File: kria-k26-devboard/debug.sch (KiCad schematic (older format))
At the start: 69 parts, among them J8 1050170001, J9 0878311420, Q10 BSS138-7-F, Q11 BSS138-7-F, Q9 BSS138-7-F, U28 MCP1799-3302H_DB, U29 MCP1799-3302H_DB, U30 FT4232HPQ, U31 93LC56CT-IMC, U32 SN74AVC4T245PWR, U33 SN74AVC4T245PWR, U34 SN74AVC2T245RSWR, U35 SN74AVC2T245RSWR, U36 NC7WZ07P6X, Y5 ABM8G-12.000MHZ-18-D2Y-T

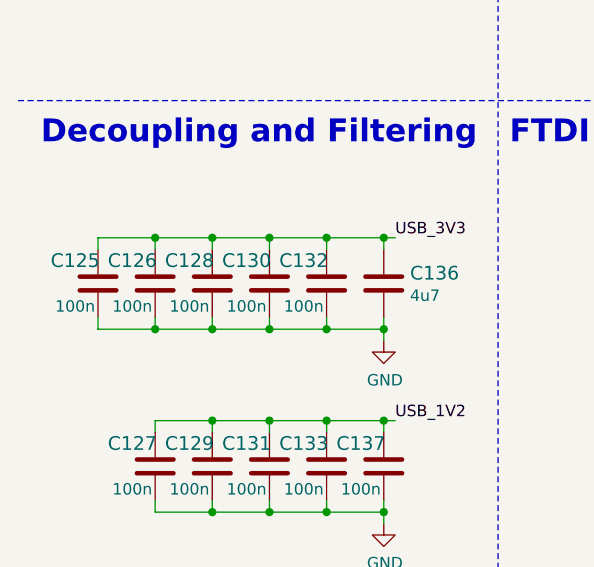
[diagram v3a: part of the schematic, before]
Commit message: Finished initial component placement
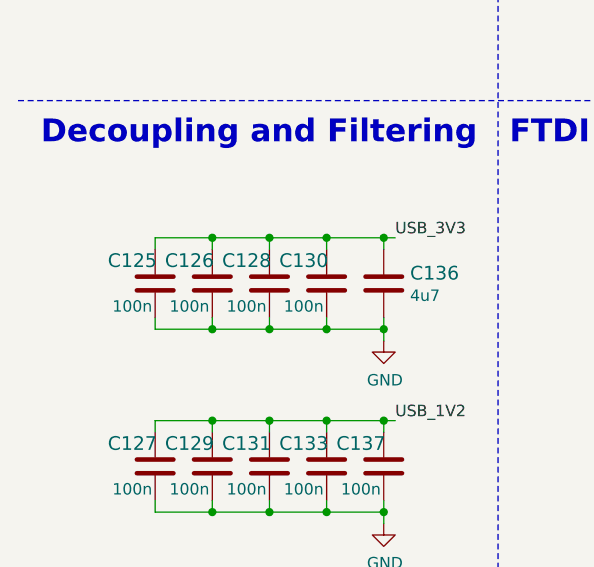
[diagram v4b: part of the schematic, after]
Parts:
- removed C132: C_100n_0402, antmicro-footprints:0402-cap, symbol antmicroCapacitors0402:C_100n_0402
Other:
- moved on the sheet: C125, C126, C128, C130
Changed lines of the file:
@@
-	0    1    1    0
-$EndComp
-$Comp
-L antmicroResistors0603:R_15k_0603 R86
-U 1 1 62B3E1B1
-P 5950 2400
-F 0 "R86" V 5905 2470 60  0000 L CNN
-F 1 "R_15k_0603" H 5950 2250 60  0001 C CNN
-F 2 "antmicro-footprints:0603-res" H 6150 2600 60  0001 L CNN
-F 3 "" H 5950 2400 50  0001 C CNN
-F 4 "BOURNS" H 6150 2800 60  0001 L CNN "Manufacturer"
-F 5 "CR0603-FX-1502ELF" H 6150 2700 60  0001 L CNN "MPN"
-F 6 "15k" V 6003 2470 50  0000 L CNN "Val"
-	1    5950 2400
 	0    1    1    0
 $EndComp
@@
 L antmicroCapacitors0402:C_100n_0402 C?
 U 1 1 62E3F1AA
-P 850 4150
+P 1100 4150
 AR Path="/63C44BC2/62E3F1AA" Ref="C?"  Part="1"
 AR Path="/63C44BC2/6235D136/62E3F1AA" Ref="C?"  Part="1"
@@
 AR Path="/63C44BC2/6244F9D5/62E3F1AA" Ref="C?"  Part="1"
 AR Path="/625B0244/62E3F1AA" Ref="C125"  Part="1"
-F 0 "C125" H 950 4050 60  0000 C CNN
-F 1 "C_100n_0402" H 850 4000 60  0001 C CNN
-F 2 "antmicro-footprints:0402-cap" H 1050 4350 60  0001 L CNN
-F 3 "" H 850 4150 50  0001 C CNN
-F 4 "Murata" H 1050 4550 60  0001 L CNN "Manufacturer"
-F 5 "GRM155R61H104KE14D" H 1050 4450 60  0001 L CNN "MPN"
-F 6 "100n" H 950 4250 50  0000 C CNN "Val"
-	1    850  4150
-	-1   0    0    1
-$EndComp
-$Comp
-L antmicroCapacitors0402:C_100n_0402 C?
-U 1 1 62E3F4A1
-P 1100 4150
-AR Path="/63C44BC2/62E3F4A1" Ref="C?"  Part="1"
-AR Path="/63C44BC2/6235D136/62E3F4A1" Ref="C?"  Part="1"
-AR Path="/63C44BC2/623E44F4/62E3F4A1" Ref="C?"  Part="1"
-AR Path="/63C44BC2/6244F9D5/62E3F4A1" Ref="C?"  Part="1"
-AR Path="/625B0244/62E3F4A1" Ref="C126"  Part="1"
-F 0 "C126" H 1200 4050 60  0000 C CNN
+F 0 "C125" H 1200 4050 60  0000 C CNN
 F 1 "C_100n_0402" H 1100 4000 60  0001 C CNN
 F 2 "antmicro-footprints:0402-cap" H 1300 4350 60  0001 L CNN
@@
 $Comp
 L antmicroCapacitors0402:C_100n_0402 C?
-U 1 1 62E3F4AE
+U 1 1 62E3F4A1
 P 1350 4150
-AR Path="/63C44BC2/62E3F4AE" Ref="C?"  Part="1"
-AR Path="/63C44BC2/6235D136/62E3F4AE" Ref="C?"  Part="1"
-AR Path="/63C44BC2/623E44F4/62E3F4AE" Ref="C?"  Part="1"
-AR Path="/63C44BC2/6244F9D5/62E3F4AE" Ref="C?"  Part="1"
-AR Path="/625B0244/62E3F4AE" Ref="C128"  Part="1"
-F 0 "C128" H 1450 4050 60  0000 C CNN
+AR Path="/63C44BC2/62E3F4A1" Ref="C?"  Part="1"
+AR Path="/63C44BC2/6235D136/62E3F4A1" Ref="C?"  Part="1"
+AR Path="/63C44BC2/623E44F4/62E3F4A1" Ref="C?"  Part="1"
+AR Path="/63C44BC2/6244F9D5/62E3F4A1" Ref="C?"  Part="1"
+AR Path="/625B0244/62E3F4A1" Ref="C126"  Part="1"
+F 0 "C126" H 1450 4050 60  0000 C CNN
 F 1 "C_100n_0402" H 1350 4000 60  0001 C CNN
 F 2 "antmicro-footprints:0402-cap" H 1550 4350 60  0001 L CNN
@@
 $Comp
 L antmicroCapacitors0402:C_100n_0402 C?
-U 1 1 62E3F4BB
+U 1 1 62E3F4AE
 P 1600 4150
-AR Path="/63C44BC2/62E3F4BB" Ref="C?"  Part="1"
-AR Path="/63C44BC2/6235D136/62E3F4BB" Ref="C?"  Part="1"
-AR Path="/63C44BC2/623E44F4/62E3F4BB" Ref="C?"  Part="1"
-AR Path="/63C44BC2/6244F9D5/62E3F4BB" Ref="C?"  Part="1"
-AR Path="/625B0244/62E3F4BB" Ref="C130"  Part="1"
-F 0 "C130" H 1700 4050 60  0000 C CNN
+AR Path="/63C44BC2/62E3F4AE" Ref="C?"  Part="1"
+AR Path="/63C44BC2/6235D136/62E3F4AE" Ref="C?"  Part="1"
+AR Path="/63C44BC2/623E44F4/62E3F4AE" Ref="C?"  Part="1"
+AR Path="/63C44BC2/6244F9D5/62E3F4AE" Ref="C?"  Part="1"
+AR Path="/625B0244/62E3F4AE" Ref="C128"  Part="1"
+F 0 "C128" H 1700 4050 60  0000 C CNN
 F 1 "C_100n_0402" H 1600 4000 60  0001 C CNN
 F 2 "antmicro-footprints:0402-cap" H 1800 4350 60  0001 L CNN
@@
 $Comp
 L antmicroCapacitors0402:C_100n_0402 C?
-U 1 1 62E3F4C8
+U 1 1 62E3F4BB
 P 1850 4150
-AR Path="/63C44BC2/62E3F4C8" Ref="C?"  Part="1"
-AR Path="/63C44BC2/6235D136/62E3F4C8" Ref="C?"  Part="1"
-AR Path="/63C44BC2/623E44F4/62E3F4C8" Ref="C?"  Part="1"
-AR Path="/63C44BC2/6244F9D5/62E3F4C8" Ref="C?"  Part="1"
-AR Path="/625B0244/62E3F4C8" Ref="C132"  Part="1"
-F 0 "C132" H 1950 4050 60  0000 C CNN
+AR Path="/63C44BC2/62E3F4BB" Ref="C?"  Part="1"
+AR Path="/63C44BC2/6235D136/62E3F4BB" Ref="C?"  Part="1"
+AR Path="/63C44BC2/623E44F4/62E3F4BB" Ref="C?"  Part="1"
+AR Path="/63C44BC2/6244F9D5/62E3F4BB" Ref="C?"  Part="1"
+AR Path="/625B0244/62E3F4BB" Ref="C130"  Part="1"
+F 0 "C130" H 1950 4050 60  0000 C CNN
 F 1 "C_100n_0402" H 1850 4000 60  0001 C CNN
 F 2 "antmicro-footprints:0402-cap" H 2050 4350 60  0001 L CNN
@@
 $EndComp
 Wire Wire Line
-	850  4000 850  3950
-Wire Wire Line
-	850  3950 1100 3950
-Wire Wire Line
-	1850 3950 1850 4000
-Wire Wire Line
-	850  4350 850  4300
-Wire Wire Line
-	850  4350 1100 4350
-Wire Wire Line
-	1850 4350 1850 4300
-Wire Wire Line
 	1100 4000 1100 3950
-Connection ~ 1100 3950
 Wire Wire Line
 	1100 3950 1350 3950
+Wire Wire Line
+	1100 4350 1100 4300
+Wire Wire Line
+	1100 4350 1350 4350
 Wire Wire Line
 	1350 4000 1350 3950
@@
 	1600 3950 1850 3950
 Wire Wire Line
-	1100 4300 1100 4350
-Connection ~ 1100 4350
-Wire Wire Line
-	1100 4350 1350 4350
+	1850 4000 1850 3950
+Connection ~ 1850 3950
 Wire Wire Line
 	1350 4300 1350 4350
@@
 	1600 4350 1850 4350
 Wire Wire Line
+	1850 4300 1850 4350
+Connection ~ 1850 4350
+Wire Wire Line
 	2100 4400 2100 4350
-Connection ~ 1850 4350
 $Comp
 L antmicroCapacitors0402:C_4u7_0402 C136
@@
 $EndComp
 Wire Wire Line
-	1850 3950 2100 3950
-Wire Wire Line
 	2100 3950 2100 4000
-Connection ~ 1850 3950
-Wire Wire Line
-	1850 4350 2100 4350
 Wire Wire Line
 	2100 4350 2100 4300
@@
 Text Label 4850 7450 2    50   ~ 0
 USB_3V3
-$Comp
-L antmicroPMICVoltageRegulatorsLinear:MCP1799-3302H_DB U29
-U 1 1 667265D6
-P 4150 2500
-F 0 "U29" H 4150 2787 60  0000 C CNN
-F 1 "MCP1799-3302H_DB" H 4150 2681 60  0000 C CNN
-F 2 "antmicro-footprints:SOT-223" H 4350 1950 60  0001 L CNN
-F 3 "https://ww1.microchip.com/downloads/en/DeviceDoc/MCP1799-Data-Sheet-20006248A.pdf" H 4350 2800 60  0001 L CNN
-F 4 "MCP1799-3302H/DB" H 4350 2050 60  0001 L CNN "MPN"
-F 5 "Microchip" H 4350 2150 60  0001 L CNN "Manufacturer"
-	1    4150 2500
-	1    0    0    -1
-$EndComp
 $Comp
 L antmicroCapacitors0603:C_10u_0603 C143
@@
 Text Notes 12250 7950 0    50   ~ 0
 A2 <- B
+Wire Wire Line
+	1850 3950 2100 3950
+Wire Wire Line
+	1850 4350 2100 4350
+$Comp
+L antmicroPMICVoltageRegulatorsLinear:MCP1799-3302H_DB U29
+U 1 1 667265D6
+P 4150 2500
+F 0 "U29" H 4150 2787 60  0000 C CNN
+F 1 "MCP1799-3302H_DB" H 4150 2681 60  0000 C CNN
+F 2 "antmicro-footprints:SOT-223" H 4350 1950 60  0001 L CNN
+F 3 "https://ww1.microchip.com/downloads/en/DeviceDoc/MCP1799-Data-Sheet-20006248A.pdf" H 4350 2800 60  0001 L CNN
+F 4 "MCP1799-3302H/DB" H 4350 2050 60  0001 L CNN "MPN"
+F 5 "Microchip" H 4350 2150 60  0001 L CNN "Manufacturer"
+	1    4150 2500
+	1    0    0    -1
+$EndComp
 Wire Bus Line
 	4700 6500 4700 6700
+$Comp
+L antmicroResistors0603:R_15k_0603 R86
+U 1 1 62B3E1B1
+P 5950 2400
+F 0 "R86" V 5905 2470 60  0000 L CNN
+F 1 "R_15k_0603" H 5950 2250 60  0001 C CNN
+F 2 "antmicro-footprints:0603-res" H 6150 2600 60  0001 L CNN
+F 3 "" H 5950 2400 50  0001 C CNN
+F 4 "BOURNS" H 6150 2800 60  0001 L CNN "Manufacturer"
+F 5 "CR0603-FX-1502ELF" H 6150 2700 60  0001 L CNN "MPN"
+F 6 "15k" V 6003 2470 50  0000 L CNN "Val"
+	1    5950 2400
+	0    1    1    0
+$EndComp
 $EndSCHEMATC

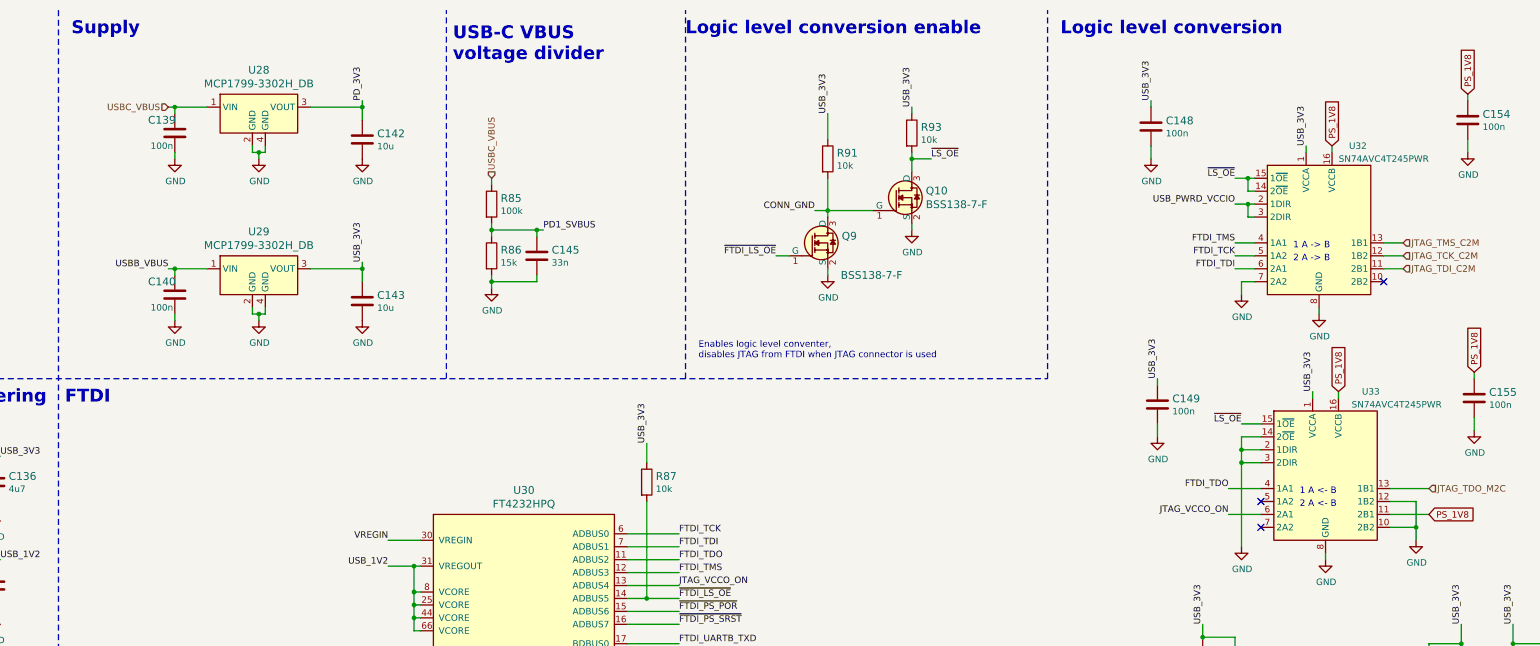
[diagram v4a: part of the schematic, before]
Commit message: Component size optimization, SOM connector fanout, routing of camera interface
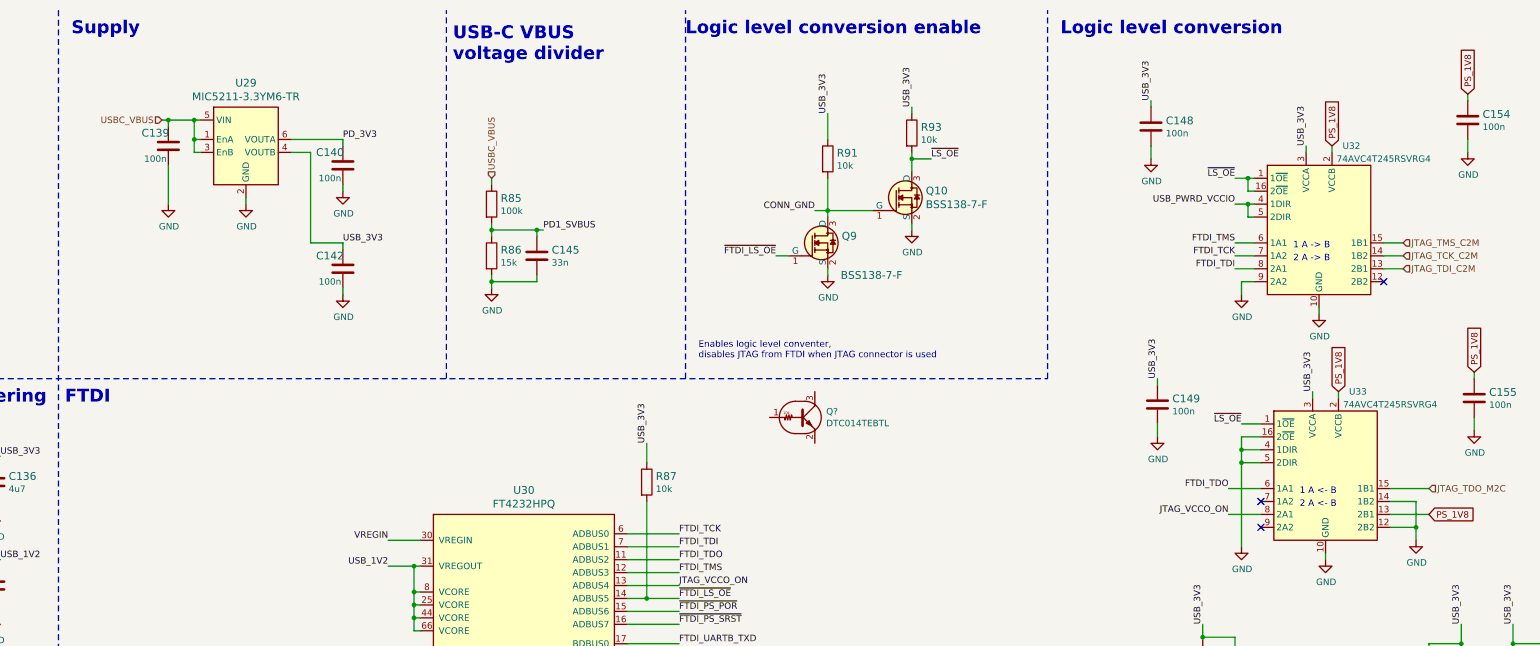
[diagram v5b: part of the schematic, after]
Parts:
- removed C142, C143: C_10u_0603, antmicro-footprints:0603-cap, symbol antmicroCapacitors0603:C_10u_0603
- removed U28, U29: MCP1799-3302H_DB, antmicro-footprints:SOT-223, symbol antmicroPMICVoltageRegulatorsLinear:MCP1799-3302H_DB
- removed U32, U33: SN74AVC4T245PWR, antmicro-footprints:TSSOP-16_4.4x5mm_P0.65mm, symbol antmicroLogicTranslatorsLevelShifters:SN74AVC4T245PWR
- added C142: C_100n_0402, antmicro-footprints:0402-cap, symbol antmicroCapacitors0402:C_100n_0402
- added Q?: DTC014TEBTL, antmicro-footprints:SOT-416, symbol antmicroTransistorsBipolarSingle:DTC014TEBTL
- added U29: MIC5211-3.3YM6-TR, antmicro-footprints:SOT-23-6, symbol antmicroPMICVoltageRegulatorsLinear:MIC5211-3.3YM6-TR
- added U32, U33: 74AVC4T245RSVRG4, antmicro-footprints:Texas_16-UFQFN, symbol antmicroLogicTranslatorsLevelShifters:74AVC4T245RSVRG4
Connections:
- net FTDI_TCK: now also U32.7 (1A2)
- net FTDI_TDI: now also U32.8 (2A1)
- net FTDI_TDO: now also U33.6 (1A1)
- net FTDI_TMS: now also U32.6 (1A1)
- net GND: now also C142.1, U29.2 (GND), U32.10 (GND), U32.11 (GND), U32.9 (2A2), U33.10 (GND), U33.11 (GND), U33.12 (2B2), U33.14 (1B2), U33.16 (2~OE), U33.4 (1DIR), U33.5 (2DIR)
- net JTAG_TCK_C2M: now also U32.14 (1B2)
- net JTAG_TDI_C2M: now also U32.13 (2B1)
- net JTAG_TDO_M2C: now also U33.15 (1B1)
- net JTAG_TMS_C2M: now also U32.15 (1B1)
- net JTAG_VCCO_ON: now also U33.8 (2A1)
- net PD_3V3: now also C140.2, U29.6 (VOUTA)
- net PS_1V8: now also U32.2 (VCCB), U33.13 (2B1), U33.2 (VCCB)
- net USBB_VBUS: no longer C140.2
- net USBC_VBUS: now also U29.1 (EnA), U29.3 (EnB), U29.5 (VIN)
- net USB_3V3: now also C142.2, U29.4 (VOUTB), U32.3 (VCCA), U33.3 (VCCA)
- net USB_PWRD_VCCIO: now also U32.4 (1DIR), U32.5 (2DIR)
- net ~LS_OE: now also U32.1 (1~OE), U32.16 (2~OE), U33.1 (1~OE)
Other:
- moved on the sheet: C139
